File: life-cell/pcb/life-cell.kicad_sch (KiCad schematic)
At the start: 4 parts

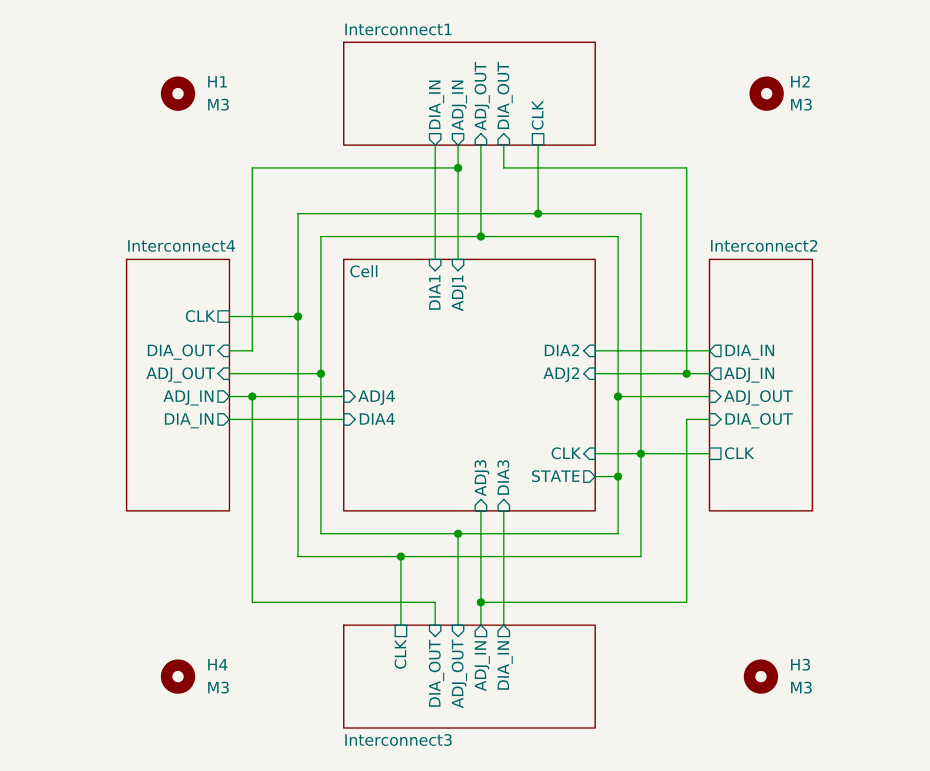
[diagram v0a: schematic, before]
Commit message: Add NSEW schem/silkscreen labels
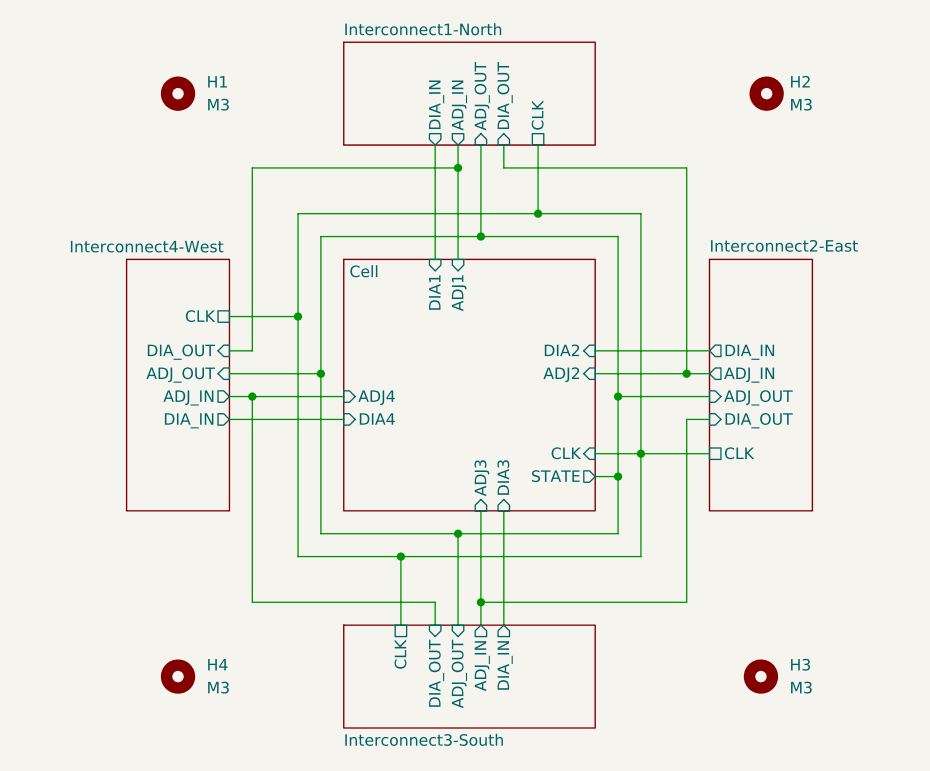
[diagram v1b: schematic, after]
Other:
- sheet Interconnect1 renamed Interconnect1-North
- sheet Interconnect2 renamed Interconnect2-East
- sheet Interconnect3 renamed Interconnect3-South
- sheet Interconnect4 renamed Interconnect4-West
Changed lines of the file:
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@@
     (stroke (width 0.1524) (type solid) (color 0 0 0 0))
     (fill (color 0 0 0 0.0000))
-    (property "Sheet name" "Interconnect1" (id 0) (at 130.81 37.465 0)
+    (property "Sheet name" "Interconnect1-North" (id 0) (at 130.81 37.465 0)
       (effects (font (size 1.27 1.27)) (justify left bottom))
     )
@@
     (stroke (width 0.1524) (type solid) (color 0 0 0 0))
     (fill (color 0 0 0 0.0000))
-    (property "Sheet name" "Interconnect2" (id 0) (at 171.45 61.5184 0)
+    (property "Sheet name" "Interconnect2-East" (id 0) (at 171.45 61.5184 0)
       (effects (font (size 1.27 1.27)) (justify left bottom))
     )
@@
     )
   )
-  (sheet (at 106.68 62.23) (size 11.43 27.94) (fields_autoplaced)
+  (sheet (at 106.68 62.23) (size 11.43 27.94)
     (stroke (width 0.1524) (type solid) (color 0 0 0 0))
     (fill (color 0 0 0 0.0000))
-    (property "Sheet name" "Interconnect4" (id 0) (at 106.68 61.5184 0)
-      (effects (font (size 1.27 1.27)) (justify left bottom))
+    (property "Sheet name" "Interconnect4-West" (id 0) (at 117.475 61.595 0)
+      (effects (font (size 1.27 1.27)) (justify right bottom))
     )
     (property "Sheet file" "Interconnect.kicad_sch" (id 1) (at 106.68 90.7546 0)
@@
     (stroke (width 0.1524) (type solid) (color 0 0 0 0))
     (fill (color 0 0 0 0.0000))
-    (property "Sheet name" "Interconnect3" (id 0) (at 130.81 114.935 0)
+    (property "Sheet name" "Interconnect3-South" (id 0) (at 130.81 114.935 0)
       (effects (font (size 1.27 1.27)) (justify left top))
     )

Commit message: Switch to "symmetric" connector layout.
Each side has half male pins and half female pins, for a truly
symmetric experience!
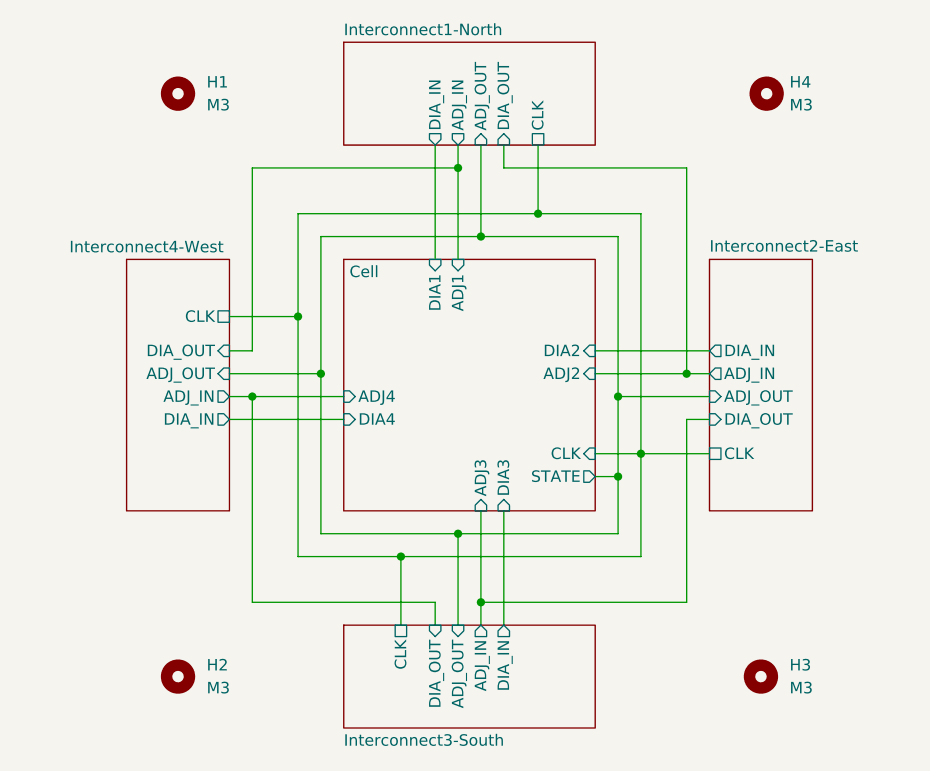
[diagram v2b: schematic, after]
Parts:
- renumbered H4 to H2, H2 to H4
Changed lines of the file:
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@@
   (symbol (lib_id "Mechanical:MountingHole") (at 177.8 43.815 0) (unit 1)
     (in_bom yes) (on_board yes) (fields_autoplaced)
-    (property "Reference" "H2" (id 0) (at 180.34 42.5449 0)
+    (property "Reference" "H4" (id 0) (at 180.34 42.5449 0)
       (effects (font (size 1.27 1.27)) (justify left))
     )
@@
   (symbol (lib_id "Mechanical:MountingHole") (at 112.395 108.585 0) (unit 1)
     (in_bom yes) (on_board yes) (fields_autoplaced)
-    (property "Reference" "H4" (id 0) (at 115.57 107.3149 0)
+    (property "Reference" "H2" (id 0) (at 115.57 107.3149 0)
       (effects (font (size 1.27 1.27)) (justify left))
     )
@@
       (reference "#PWR010") (unit 1) (value "GND") (footprint "")
     )
+    (path "/19454d8c-8b20-4896-a5b1-cefbf4f83cbc/c806bfc4-efeb-4804-9cb9-cc167cb8f885"
+      (reference "#PWR011") (unit 1) (value "GND") (footprint "")
+    )
     (path "/19454d8c-8b20-4896-a5b1-cefbf4f83cbc/b8d0bd1a-48e1-4954-88d9-39ad08081272"
-      (reference "#PWR011") (unit 1) (value "VCC") (footprint "")
-    )
-    (path "/19454d8c-8b20-4896-a5b1-cefbf4f83cbc/c806bfc4-efeb-4804-9cb9-cc167cb8f885"
-      (reference "#PWR012") (unit 1) (value "GND") (footprint "")
+      (reference "#PWR012") (unit 1) (value "VCC") (footprint "")
+    )
+    (path "/94b771bd-5699-4af4-9031-2a3069c4f4d1/c806bfc4-efeb-4804-9cb9-cc167cb8f885"
+      (reference "#PWR013") (unit 1) (value "GND") (footprint "")
     )
     (path "/94b771bd-5699-4af4-9031-2a3069c4f4d1/b8d0bd1a-48e1-4954-88d9-39ad08081272"
-      (reference "#PWR013") (unit 1) (value "VCC") (footprint "")
-    )
-    (path "/94b771bd-5699-4af4-9031-2a3069c4f4d1/c806bfc4-efeb-4804-9cb9-cc167cb8f885"
-      (reference "#PWR014") (unit 1) (value "GND") (footprint "")
+      (reference "#PWR014") (unit 1) (value "VCC") (footprint "")
+    )
+    (path "/bb158afa-1fbd-4063-ab33-621e2af4a5c4/c806bfc4-efeb-4804-9cb9-cc167cb8f885"
+      (reference "#PWR015") (unit 1) (value "GND") (footprint "")
     )
     (path "/bb158afa-1fbd-4063-ab33-621e2af4a5c4/b8d0bd1a-48e1-4954-88d9-39ad08081272"
-      (reference "#PWR015") (unit 1) (value "VCC") (footprint "")
-    )
-    (path "/bb158afa-1fbd-4063-ab33-621e2af4a5c4/c806bfc4-efeb-4804-9cb9-cc167cb8f885"
-      (reference "#PWR016") (unit 1) (value "GND") (footprint "")
+      (reference "#PWR016") (unit 1) (value "VCC") (footprint "")
+    )
+    (path "/7b525188-5e2d-49d9-a447-2c95c7d3ce38/c806bfc4-efeb-4804-9cb9-cc167cb8f885"
+      (reference "#PWR017") (unit 1) (value "GND") (footprint "")
     )
     (path "/7b525188-5e2d-49d9-a447-2c95c7d3ce38/b8d0bd1a-48e1-4954-88d9-39ad08081272"
-      (reference "#PWR017") (unit 1) (value "VCC") (footprint "")
-    )
-    (path "/7b525188-5e2d-49d9-a447-2c95c7d3ce38/c806bfc4-efeb-4804-9cb9-cc167cb8f885"
-      (reference "#PWR018") (unit 1) (value "GND") (footprint "")
+      (reference "#PWR018") (unit 1) (value "VCC") (footprint "")
     )
     (path "/98d822a1-05f6-4a90-84ca-6893c8a1545a/0431cac5-da99-4dbc-86ad-1b5a0bf261ba"
@@
       (reference "H1") (unit 1) (value "M3") (footprint "MountingHole:MountingHole_3.2mm_M3_Pad")
     )
-    (path "/54142e38-446b-46d0-8581-4012910e390e"
+    (path "/aa5c31cb-c19e-4d8f-98ac-7f2eb7a11121"
       (reference "H2") (unit 1) (value "M3") (footprint "MountingHole:MountingHole_3.2mm_M3_Pad")
     )
@@
       (reference "H3") (unit 1) (value "M3") (footprint "MountingHole:MountingHole_3.2mm_M3_Pad")
     )
-    (path "/aa5c31cb-c19e-4d8f-98ac-7f2eb7a11121"
+    (path "/54142e38-446b-46d0-8581-4012910e390e"
       (reference "H4") (unit 1) (value "M3") (footprint "MountingHole:MountingHole_3.2mm_M3_Pad")
     )
-    (path "/19454d8c-8b20-4896-a5b1-cefbf4f83cbc/b60b7348-62ea-4008-95be-9e6eab2cdd9a"
-      (reference "J1") (unit 1) (value "Interconnect") (footprint "Connector_PinHeader_2.54mm:PinHeader_1x10_P2.54mm_Vertical")
-    )
-    (path "/7b525188-5e2d-49d9-a447-2c95c7d3ce38/b60b7348-62ea-4008-95be-9e6eab2cdd9a"
-      (reference "J2") (unit 1) (value "Interconnect") (footprint "Connector_PinHeader_2.54mm:PinHeader_1x10_P2.54mm_Vertical")
-    )
-    (path "/bb158afa-1fbd-4063-ab33-621e2af4a5c4/b60b7348-62ea-4008-95be-9e6eab2cdd9a"
-      (reference "J3") (unit 1) (value "Interconnect") (footprint "Connector_PinHeader_2.54mm:PinHeader_1x10_P2.54mm_Vertical")
-    )
-    (path "/94b771bd-5699-4af4-9031-2a3069c4f4d1/b60b7348-62ea-4008-95be-9e6eab2cdd9a"
-      (reference "J4") (unit 1) (value "Interconnect") (footprint "Connector_PinHeader_2.54mm:PinHeader_1x10_P2.54mm_Vertical")
-    )
     (path "/98d822a1-05f6-4a90-84ca-6893c8a1545a/d66d863c-d696-4d5b-9cb4-c58666da6717"
-      (reference "J5") (unit 1) (value "UPDI") (footprint "Connector_PinHeader_2.54mm:PinHeader_1x03_P2.54mm_Vertical")
+      (reference "J1") (unit 1) (value "UPDI") (footprint "Connector_PinHeader_2.54mm:PinHeader_1x03_P2.54mm_Vertical")
+    )
+    (path "/19454d8c-8b20-4896-a5b1-cefbf4f83cbc/cb780aa4-6cec-4f85-87d0-bc0b0824e017"
+      (reference "J2") (unit 1) (value "Interconnect In") (footprint "Connector_PinHeader_2.54mm:PinHeader_1x05_P2.54mm_Horizontal")
+    )
+    (path "/19454d8c-8b20-4896-a5b1-cefbf4f83cbc/ad3e5386-b9b9-4f0d-a2e0-4c291a944f14"
+      (reference "J3") (unit 1) (value "Interconnect Out") (footprint "Connector_PinSocket_2.54mm:PinSocket_1x05_P2.54mm_Horizontal")
+    )
+    (path "/94b771bd-5699-4af4-9031-2a3069c4f4d1/cb780aa4-6cec-4f85-87d0-bc0b0824e017"
+      (reference "J4") (unit 1) (value "Interconnect In") (footprint "Connector_PinHeader_2.54mm:PinHeader_1x05_P2.54mm_Horizontal")
+    )
+    (path "/94b771bd-5699-4af4-9031-2a3069c4f4d1/ad3e5386-b9b9-4f0d-a2e0-4c291a944f14"
+      (reference "J5") (unit 1) (value "Interconnect Out") (footprint "Connector_PinSocket_2.54mm:PinSocket_1x05_P2.54mm_Horizontal")
+    )
+    (path "/bb158afa-1fbd-4063-ab33-621e2af4a5c4/cb780aa4-6cec-4f85-87d0-bc0b0824e017"
+      (reference "J6") (unit 1) (value "Interconnect In") (footprint "Connector_PinHeader_2.54mm:PinHeader_1x05_P2.54mm_Horizontal")
+    )
+    (path "/bb158afa-1fbd-4063-ab33-621e2af4a5c4/ad3e5386-b9b9-4f0d-a2e0-4c291a944f14"
+      (reference "J7") (unit 1) (value "Interconnect Out") (footprint "Connector_PinSocket_2.54mm:PinSocket_1x05_P2.54mm_Horizontal")
+    )
+    (path "/7b525188-5e2d-49d9-a447-2c95c7d3ce38/cb780aa4-6cec-4f85-87d0-bc0b0824e017"
+      (reference "J8") (unit 1) (value "Interconnect In") (footprint "Connector_PinHeader_2.54mm:PinHeader_1x05_P2.54mm_Horizontal")
+    )
+    (path "/7b525188-5e2d-49d9-a447-2c95c7d3ce38/ad3e5386-b9b9-4f0d-a2e0-4c291a944f14"
+      (reference "J9") (unit 1) (value "Interconnect Out") (footprint "Connector_PinSocket_2.54mm:PinSocket_1x05_P2.54mm_Horizontal")
     )
     (path "/98d822a1-05f6-4a90-84ca-6893c8a1545a/262fc697-1107-46a7-a0b8-767a450e6a46"
